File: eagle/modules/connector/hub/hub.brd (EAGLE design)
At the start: 59.7 x 14.3 mm, 4 parts

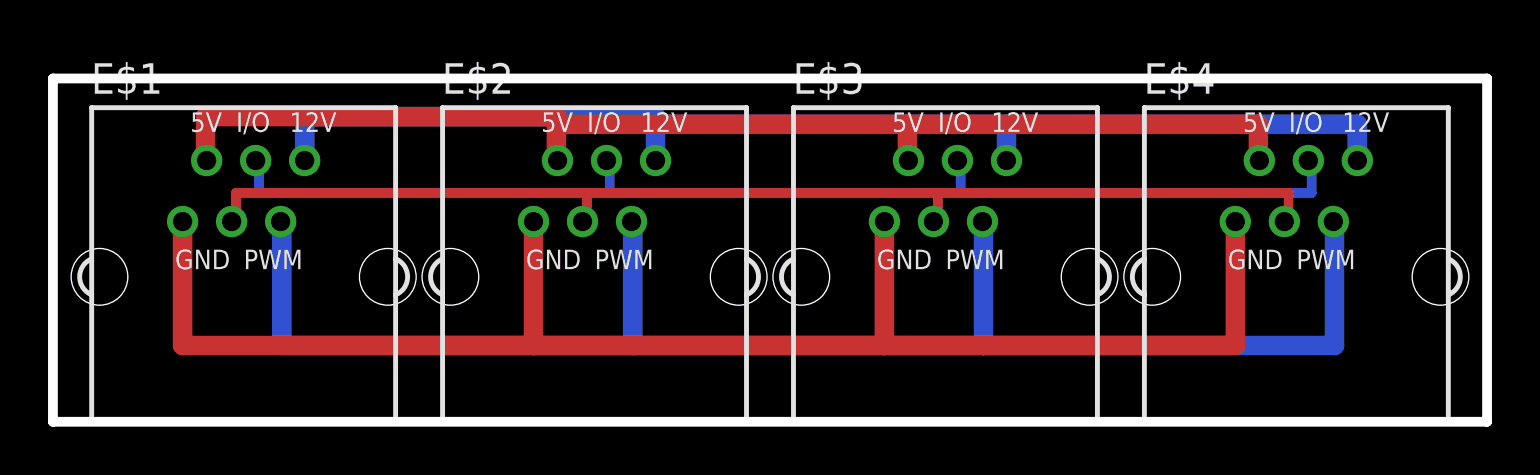
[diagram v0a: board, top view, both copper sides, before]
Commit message: Improve sound
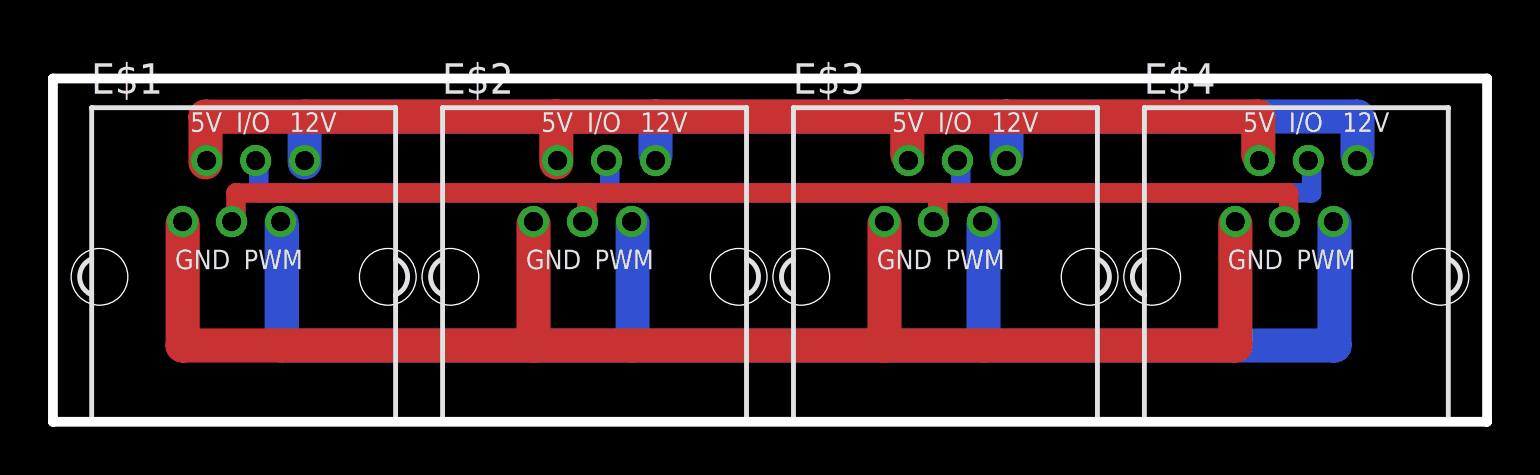
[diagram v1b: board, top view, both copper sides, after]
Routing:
- net S$8: track 50.2 -> 50.8 mm
- net S$7: track 49.8 -> 50.5 mm
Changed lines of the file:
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@@
 <?xml version="1.0" encoding="utf-8"?>
 <!DOCTYPE eagle SYSTEM "eagle.dtd">
-<eagle version="6.1">
+<eagle version="7.1.0">
 <drawing>
 <settings>
@@
 </class>
 </classes>
-<designrules>
+<designrules name="default">
 <description language="de">&lt;b&gt;EAGLE Design Rules&lt;/b&gt;
 &lt;p&gt;
@@
 <pass name="Default">
 <param name="RoutingGrid" value="50mil"/>
+<param name="AutoGrid" value="1"/>
+<param name="Efforts" value="0"/>
+<param name="TopRouterVariant" value="1"/>
 <param name="tpViaShape" value="round"/>
 <param name="PrefDir.1" value="-"/>
@@
 </signal>
 <signal name="S$7">
-<wire x1="11.1125" y1="10.795" x2="11.1125" y2="12.7" width="0.8128" layer="16"/>
-<wire x1="11.1125" y1="12.7" x2="25.7175" y2="12.7" width="0.8128" layer="16"/>
-<wire x1="25.7175" y1="12.7" x2="25.7175" y2="12.3825" width="0.8128" layer="16"/>
-<wire x1="25.7175" y1="11.1125" x2="25.7175" y2="12.3825" width="0.8128" layer="16"/>
-<wire x1="25.7175" y1="12.3825" x2="40.3225" y2="12.3825" width="0.8128" layer="16"/>
-<wire x1="40.3225" y1="11.1125" x2="40.3225" y2="12.3825" width="0.8128" layer="16"/>
-<wire x1="40.3225" y1="12.3825" x2="54.9275" y2="12.3825" width="0.8128" layer="16"/>
-<wire x1="54.9275" y1="12.3825" x2="54.9275" y2="11.1125" width="0.8128" layer="16"/>
+<wire x1="11.1125" y1="10.795" x2="11.1125" y2="12.7" width="1.4224" layer="16"/>
+<wire x1="11.1125" y1="12.7" x2="25.7175" y2="12.7" width="1.4224" layer="16"/>
+<wire x1="25.7175" y1="11.1125" x2="25.7175" y2="12.7" width="1.4224" layer="16"/>
+<wire x1="25.7175" y1="12.7" x2="40.3225" y2="12.7" width="1.4224" layer="16"/>
+<wire x1="40.3225" y1="11.1125" x2="40.3225" y2="12.7" width="1.4224" layer="16"/>
+<wire x1="40.3225" y1="12.7" x2="54.9275" y2="12.7" width="1.4224" layer="16"/>
+<wire x1="54.9275" y1="12.7" x2="54.9275" y2="11.1125" width="1.4224" layer="16"/>
 </signal>
 <signal name="S$8">
-<wire x1="6.985" y1="10.795" x2="6.985" y2="12.7" width="0.8128" layer="1"/>
-<wire x1="6.985" y1="12.7" x2="21.59" y2="12.7" width="0.8128" layer="1"/>
-<wire x1="21.59" y1="12.7" x2="21.59" y2="12.3825" width="0.8128" layer="1"/>
-<wire x1="21.59" y1="10.795" x2="21.59" y2="12.3825" width="0.8128" layer="1"/>
-<wire x1="21.59" y1="12.3825" x2="36.195" y2="12.3825" width="0.8128" layer="1"/>
-<wire x1="36.195" y1="11.1125" x2="36.195" y2="12.3825" width="0.8128" layer="1"/>
-<wire x1="36.195" y1="12.3825" x2="50.8" y2="12.3825" width="0.8128" layer="1"/>
-<wire x1="50.8" y1="12.3825" x2="50.8" y2="11.1125" width="0.8128" layer="1"/>
+<wire x1="6.985" y1="10.795" x2="6.985" y2="12.7" width="1.4224" layer="1"/>
+<wire x1="6.985" y1="12.7" x2="21.59" y2="12.7" width="1.4224" layer="1"/>
+<wire x1="21.59" y1="10.795" x2="21.59" y2="12.7" width="1.4224" layer="1"/>
+<wire x1="21.59" y1="12.7" x2="36.195" y2="12.7" width="1.4224" layer="1"/>
+<wire x1="36.195" y1="11.1125" x2="36.195" y2="12.7" width="1.4224" layer="1"/>
+<wire x1="36.195" y1="12.7" x2="50.8" y2="12.7" width="1.4224" layer="1"/>
+<wire x1="50.8" y1="12.7" x2="50.8" y2="11.1125" width="1.4224" layer="1"/>
 </signal>
 <signal name="S$9">
-<wire x1="6.0325" y1="8.255" x2="6.0325" y2="3.175" width="0.8128" layer="1"/>
-<wire x1="6.0325" y1="3.175" x2="20.6375" y2="3.175" width="0.8128" layer="1"/>
-<wire x1="20.6375" y1="8.255" x2="20.6375" y2="3.175" width="0.8128" layer="1"/>
-<wire x1="20.6375" y1="3.175" x2="35.2425" y2="3.175" width="0.8128" layer="1"/>
-<wire x1="35.2425" y1="8.255" x2="35.2425" y2="3.175" width="0.8128" layer="1"/>
-<wire x1="35.2425" y1="3.175" x2="49.8475" y2="3.175" width="0.8128" layer="1"/>
-<wire x1="49.8475" y1="3.175" x2="49.8475" y2="8.255" width="0.8128" layer="1"/>
+<wire x1="6.0325" y1="8.255" x2="6.0325" y2="3.175" width="1.4224" layer="1"/>
+<wire x1="6.0325" y1="3.175" x2="20.6375" y2="3.175" width="1.4224" layer="1"/>
+<wire x1="20.6375" y1="8.255" x2="20.6375" y2="3.175" width="1.4224" layer="1"/>
+<wire x1="20.6375" y1="3.175" x2="35.2425" y2="3.175" width="1.4224" layer="1"/>
+<wire x1="35.2425" y1="8.255" x2="35.2425" y2="3.175" width="1.4224" layer="1"/>
+<wire x1="35.2425" y1="3.175" x2="49.8475" y2="3.175" width="1.4224" layer="1"/>
+<wire x1="49.8475" y1="3.175" x2="49.8475" y2="8.255" width="1.4224" layer="1"/>
 </signal>
 <signal name="S$10">
-<wire x1="10.16" y1="8.255" x2="10.16" y2="3.175" width="0.8128" layer="16"/>
-<wire x1="10.16" y1="3.175" x2="24.765" y2="3.175" width="0.8128" layer="16"/>
-<wire x1="24.765" y1="8.255" x2="24.765" y2="3.175" width="0.8128" layer="16"/>
-<wire x1="24.765" y1="3.175" x2="39.37" y2="3.175" width="0.8128" layer="16"/>
-<wire x1="39.37" y1="8.255" x2="39.37" y2="3.175" width="0.8128" layer="16"/>
-<wire x1="39.37" y1="3.175" x2="53.975" y2="3.175" width="0.8128" layer="16"/>
-<wire x1="53.975" y1="3.175" x2="53.975" y2="8.255" width="0.8128" layer="16"/>
+<wire x1="10.16" y1="8.255" x2="10.16" y2="3.175" width="1.4224" layer="16"/>
+<wire x1="10.16" y1="3.175" x2="24.765" y2="3.175" width="1.4224" layer="16"/>
+<wire x1="24.765" y1="8.255" x2="24.765" y2="3.175" width="1.4224" layer="16"/>
+<wire x1="24.765" y1="3.175" x2="39.37" y2="3.175" width="1.4224" layer="16"/>
+<wire x1="39.37" y1="8.255" x2="39.37" y2="3.175" width="1.4224" layer="16"/>
+<wire x1="39.37" y1="3.175" x2="53.975" y2="3.175" width="1.4224" layer="16"/>
+<wire x1="53.975" y1="3.175" x2="53.975" y2="8.255" width="1.4224" layer="16"/>
 </signal>
 <signal name="S$11">
-<wire x1="9.2075" y1="10.795" x2="9.2075" y2="9.525" width="0.4064" layer="16"/>
-<wire x1="9.2075" y1="9.525" x2="23.8125" y2="9.525" width="0.4064" layer="16"/>
-<wire x1="23.8125" y1="10.795" x2="23.8125" y2="9.525" width="0.4064" layer="16"/>
-<wire x1="23.8125" y1="9.525" x2="38.4175" y2="9.525" width="0.4064" layer="16"/>
-<wire x1="38.4175" y1="10.795" x2="38.4175" y2="9.525" width="0.4064" layer="16"/>
-<wire x1="38.4175" y1="9.525" x2="53.0225" y2="9.525" width="0.4064" layer="16"/>
-<wire x1="53.0225" y1="9.525" x2="53.0225" y2="10.795" width="0.4064" layer="16"/>
+<wire x1="9.2075" y1="10.795" x2="9.2075" y2="9.525" width="0.8128" layer="16"/>
+<wire x1="9.2075" y1="9.525" x2="23.8125" y2="9.525" width="0.8128" layer="16"/>
+<wire x1="23.8125" y1="10.795" x2="23.8125" y2="9.525" width="0.8128" layer="16"/>
+<wire x1="23.8125" y1="9.525" x2="38.4175" y2="9.525" width="0.8128" layer="16"/>
+<wire x1="38.4175" y1="10.795" x2="38.4175" y2="9.525" width="0.8128" layer="16"/>
+<wire x1="38.4175" y1="9.525" x2="53.0225" y2="9.525" width="0.8128" layer="16"/>
+<wire x1="53.0225" y1="9.525" x2="53.0225" y2="10.795" width="0.8128" layer="16"/>
 </signal>
 <signal name="S$12">
-<wire x1="8.255" y1="8.255" x2="8.255" y2="9.525" width="0.4064" layer="1"/>
-<wire x1="8.255" y1="9.525" x2="22.86" y2="9.525" width="0.4064" layer="1"/>
-<wire x1="22.86" y1="8.255" x2="22.86" y2="9.525" width="0.4064" layer="1"/>
-<wire x1="22.86" y1="9.525" x2="37.465" y2="9.525" width="0.4064" layer="1"/>
-<wire x1="37.465" y1="8.255" x2="37.465" y2="9.525" width="0.4064" layer="1"/>
-<wire x1="37.465" y1="9.525" x2="52.07" y2="9.525" width="0.4064" layer="1"/>
-<wire x1="52.07" y1="9.525" x2="52.07" y2="8.255" width="0.4064" layer="1"/>
+<wire x1="8.255" y1="8.255" x2="8.255" y2="9.525" width="0.8128" layer="1"/>
+<wire x1="8.255" y1="9.525" x2="22.86" y2="9.525" width="0.8128" layer="1"/>
+<wire x1="22.86" y1="8.255" x2="22.86" y2="9.525" width="0.8128" layer="1"/>
+<wire x1="22.86" y1="9.525" x2="37.465" y2="9.525" width="0.8128" layer="1"/>
+<wire x1="37.465" y1="8.255" x2="37.465" y2="9.525" width="0.8128" layer="1"/>
+<wire x1="37.465" y1="9.525" x2="52.07" y2="9.525" width="0.8128" layer="1"/>
+<wire x1="52.07" y1="9.525" x2="52.07" y2="8.255" width="0.8128" layer="1"/>
 </signal>
 </signals>
